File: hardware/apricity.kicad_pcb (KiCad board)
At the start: 2 copper layers, 71.2 x 71.2 mm, 21 parts, among them J1 USB_C_Receptacle_USB2.0, U1 ESP-WROOM-02D

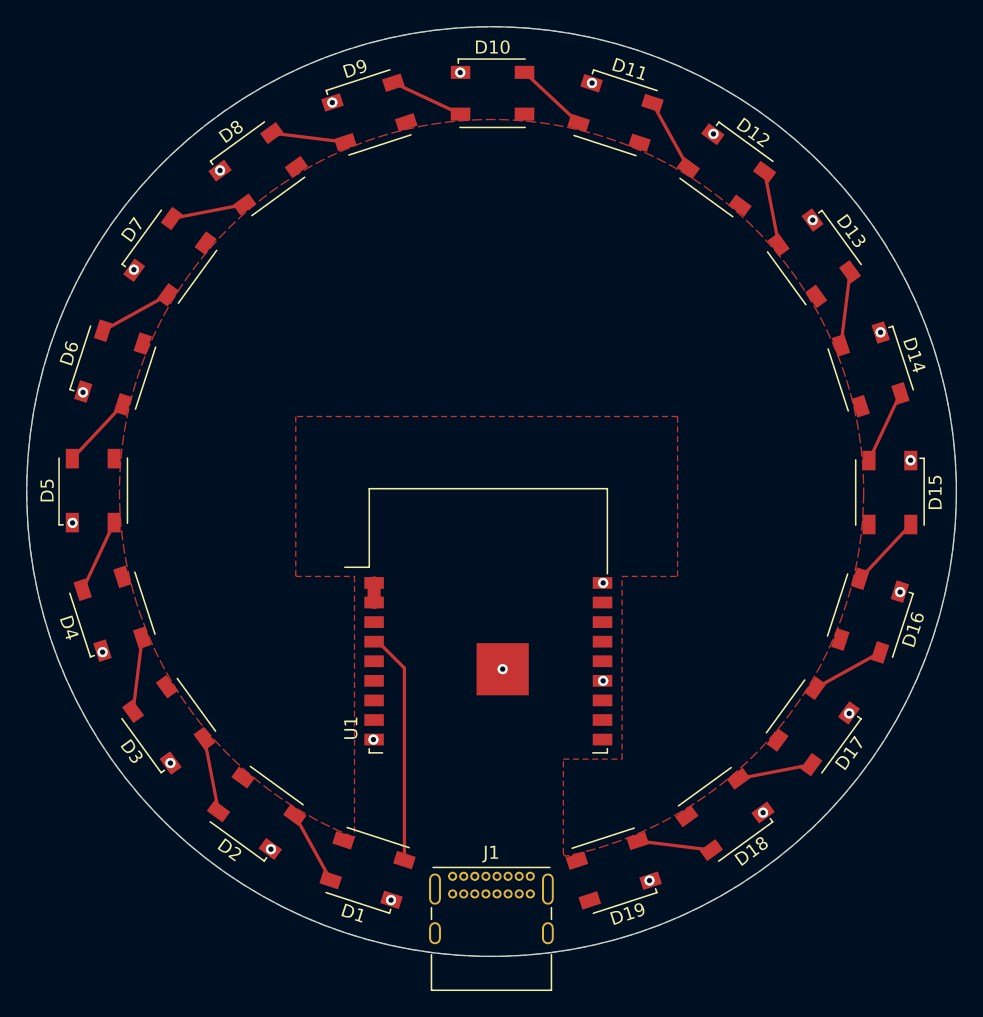
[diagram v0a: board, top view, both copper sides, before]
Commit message: fix power plane and add room for components
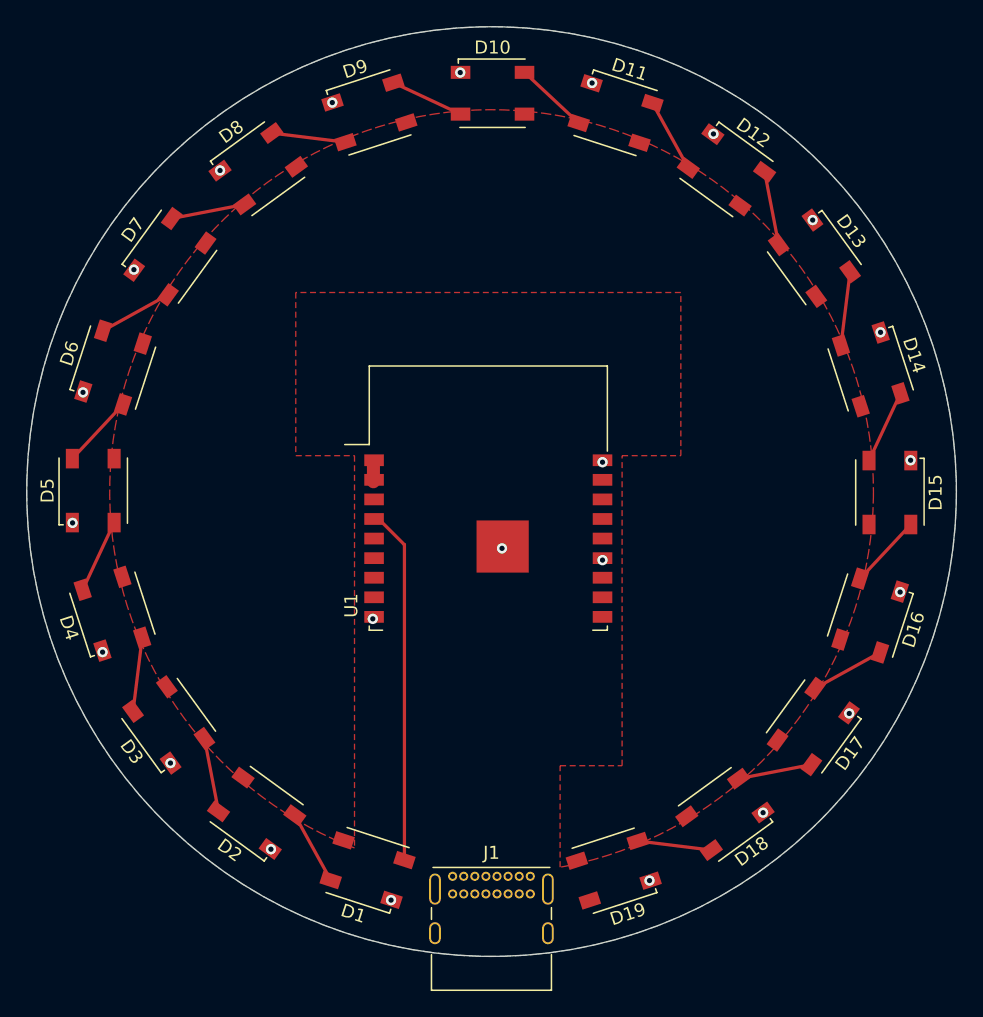
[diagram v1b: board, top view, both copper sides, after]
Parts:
- moved U1 9.40 mm to (147.8, 97.6)
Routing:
- net /LED: track 17.9 -> 27.6 mm
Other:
- board text added: "Apricity (Revision A) J. L. Hay https://jordanhay.com/"
- board text removed: "The Apricity Light J. L. Hay https://jordanhay.com/"

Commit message: Annotate schematic and add power components
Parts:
- added R1: 5.1k, Resistor_SMD:R_0805_2012Metric, F.Cu at (146.0, 118.0)
- added R2: 5.1k, Resistor_SMD:R_0805_2012Metric, F.Cu at (150.4, 118.0)
- added U2: X, Package_TO_SOT_SMD:TSOT-23_HandSoldering, F.Cu at (148.0, 111.0)
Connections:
- J1 pad A4: Net-(J1-PadA4) -> +5V
- J1 pad A9: Net-(J1-PadA4) -> +5V
- J1 pad B4: Net-(J1-PadA4) -> +5V
- J1 pad B9: Net-(J1-PadA4) -> +5V
- J1 pad S1: unconnected-(J1-PadS1) -> Net-(J1-PadS1)

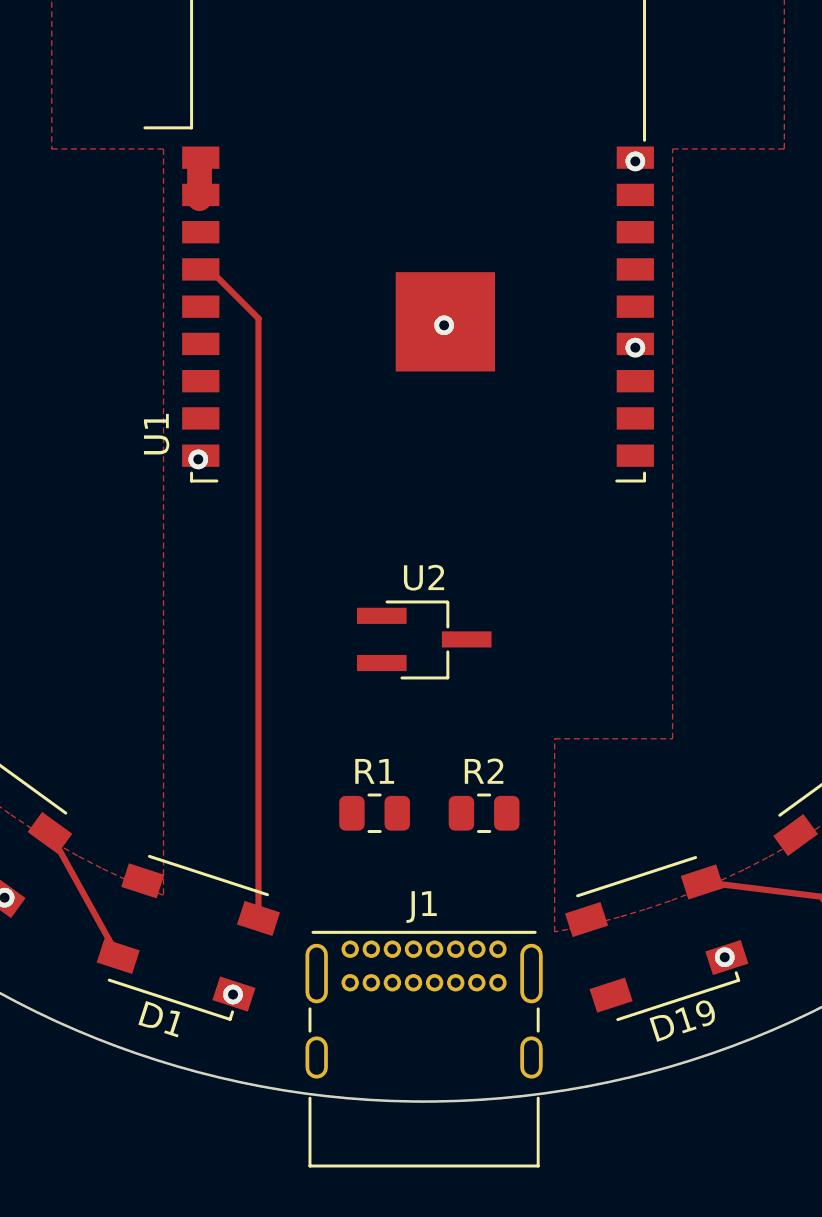
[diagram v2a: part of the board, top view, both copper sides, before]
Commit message: layout power components on pcb
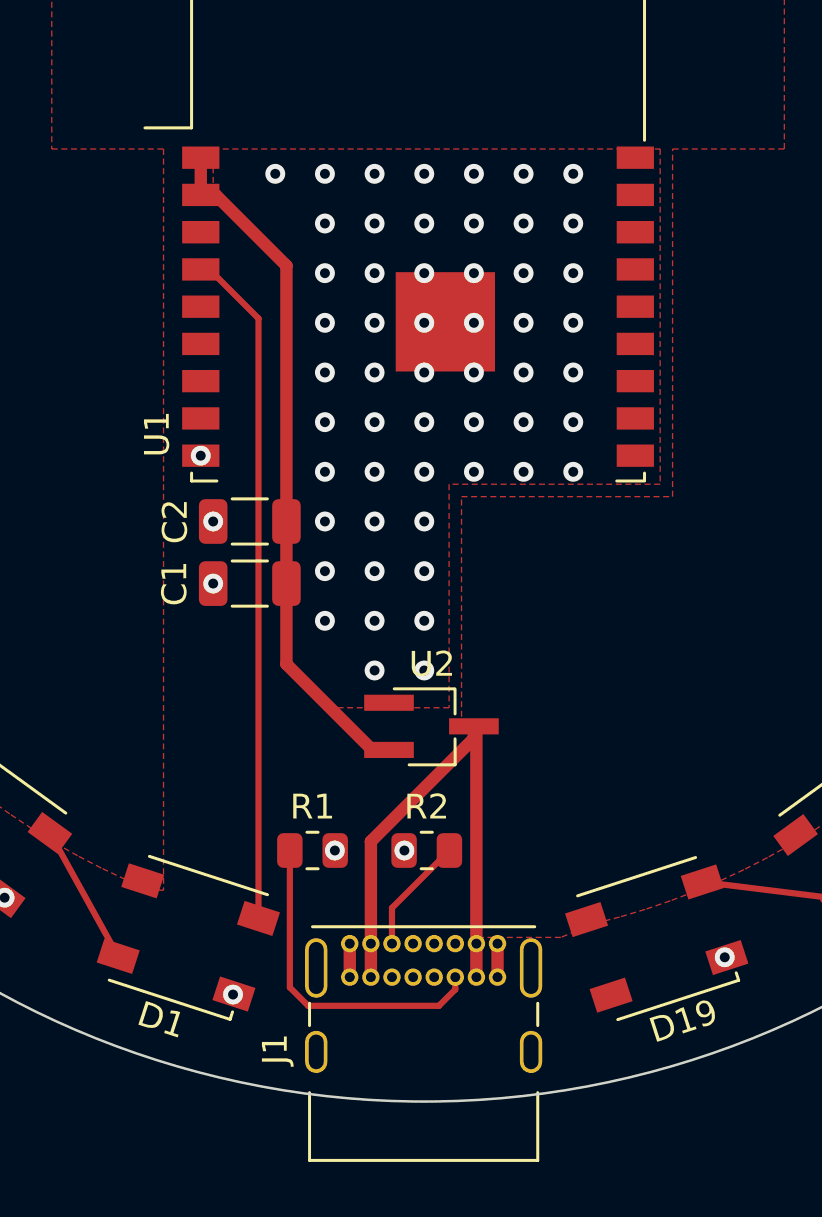
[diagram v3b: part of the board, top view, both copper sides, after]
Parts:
- added C1: 0.1u, Capacitor_SMD:C_1206_3216Metric, F.Cu at (141.0, 108.8)
- added C2: 10u, Capacitor_SMD:C_1206_3216Metric, F.Cu at (141.0, 106.2)
- moved U2 3.51 mm to (148.3, 114.5)
- moved R1 2.92 mm to (143.5, 119.5)
- moved R2 2.75 mm to (148.1, 119.5), turned to 180 degrees
- moved J1 0.23 mm to (145.0, 123.2)
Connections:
- J1 pad S1: Net-(J1-PadS1) -> unconnected-(J1-PadS1)
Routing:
- net +3.3V: track 1.50 -> 27.7 mm
- net +5V: track 0.00 -> 22.0 mm
- net Net-(J1-PadB5): track 0.00 -> 13.3 mm
- net Net-(J1-PadA5): track 0.00 -> 4.71 mm
- net GND: track 0.00 -> 2.70 mm, vias 23 -> 78
- added copper zone on F.Cu, net GND

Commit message: Play with power planes
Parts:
- J1: footprint Connector_USB:USB_C_Receptacle_GCT_USB4085 -> Connector_USB:USB_C_Receptacle_Palconn_UTC16-G
- moved R1 5.44 mm to (148.9, 120.2), turned to 90 degrees
- moved J1 3.75 mm to (147.9, 125.6)
- moved C1 3.05 mm to (144.0, 108.8), turned to 0 degrees
- moved C2 3.03 mm to (144.0, 106.2), turned to 0 degrees
- moved R2 1.48 mm to (146.8, 120.2), turned to 90 degrees
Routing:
- net Net-(J1-PadB5): track 13.3 -> 2.32 mm
- net +5V: track 22.0 -> 26.2 mm
- net Net-(J1-PadA5): track 4.71 -> 2.06 mm
- net GND: track 2.70 -> 4.29 mm

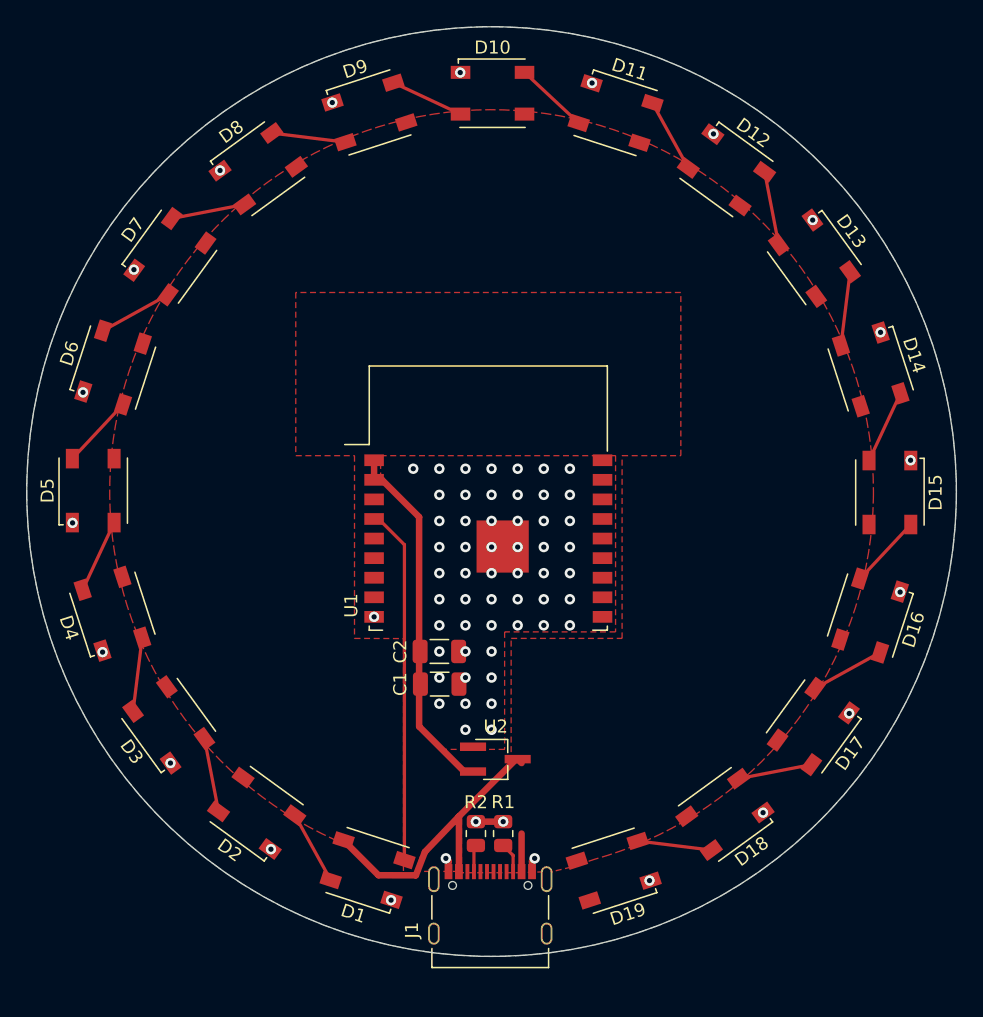
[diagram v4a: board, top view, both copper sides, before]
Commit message: re-arrange power components
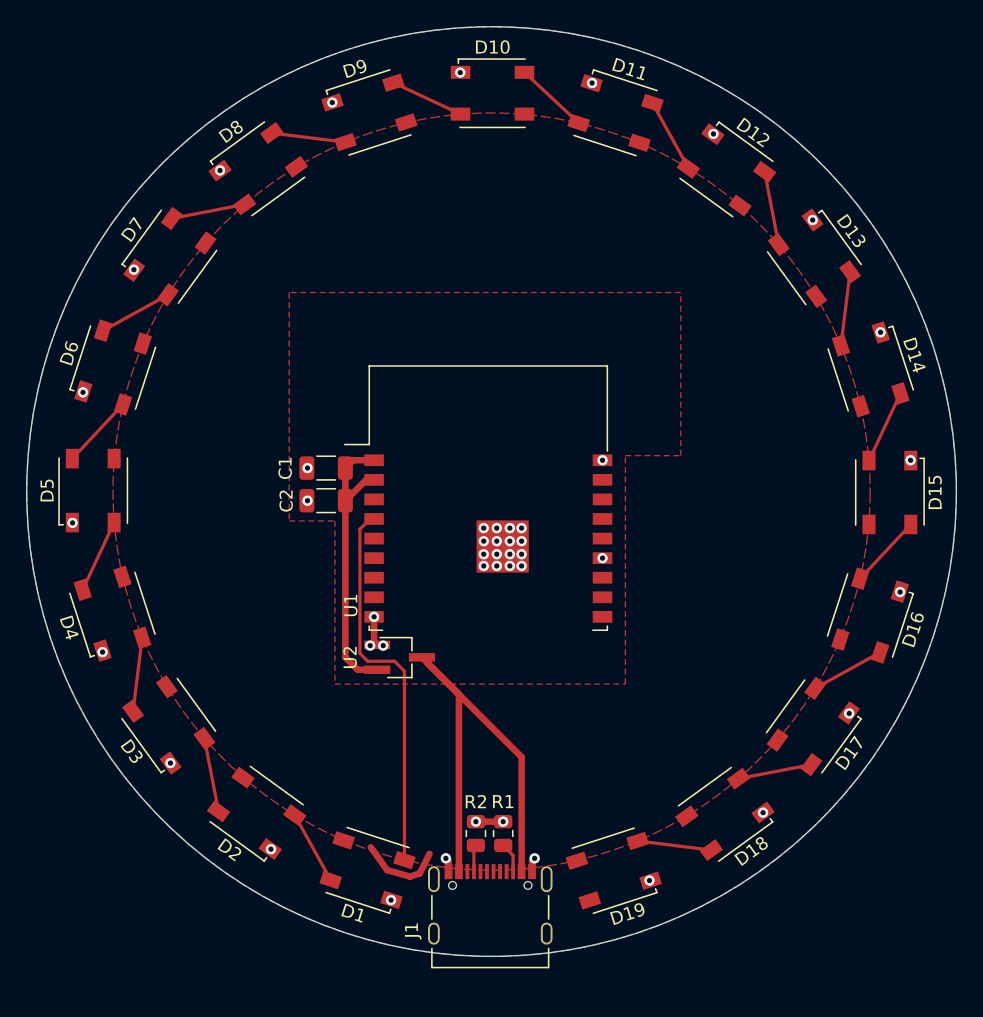
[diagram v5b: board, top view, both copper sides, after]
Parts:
- moved C1 18.7 mm to (135.3, 92.2), turned to 180 degrees
- moved C2 14.4 mm to (135.3, 94.7), turned to 180 degrees
- moved U2 10.7 mm to (140.9, 106.7)
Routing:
- net +5V: track 26.2 -> 43.0 mm
- net +3.3V: track 27.7 -> 22.7 mm
- net GND: track 4.29 -> 6.54 mm, vias 78 -> 46
- net /LED: track 27.6 -> 29.7 mm
- removed copper zone on F.Cu, net GND
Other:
- board text added: "Apricity J. L. Hay https://jordanhay.com/ Revision A"
- board text removed: "Apricity (Revision A) J. L. Hay https://jordanhay.com/"
